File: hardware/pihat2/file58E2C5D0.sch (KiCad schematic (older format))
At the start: 45 parts, among them P1 USB_OTG, P2 BATT, P3 THERM, U1 MCP73833, U2 SMA_Edge_Mount, U3 SMA_Edge_Mount, U4 TPS61027, U5 MCP3021, U6 Si4464, U7 30MHz

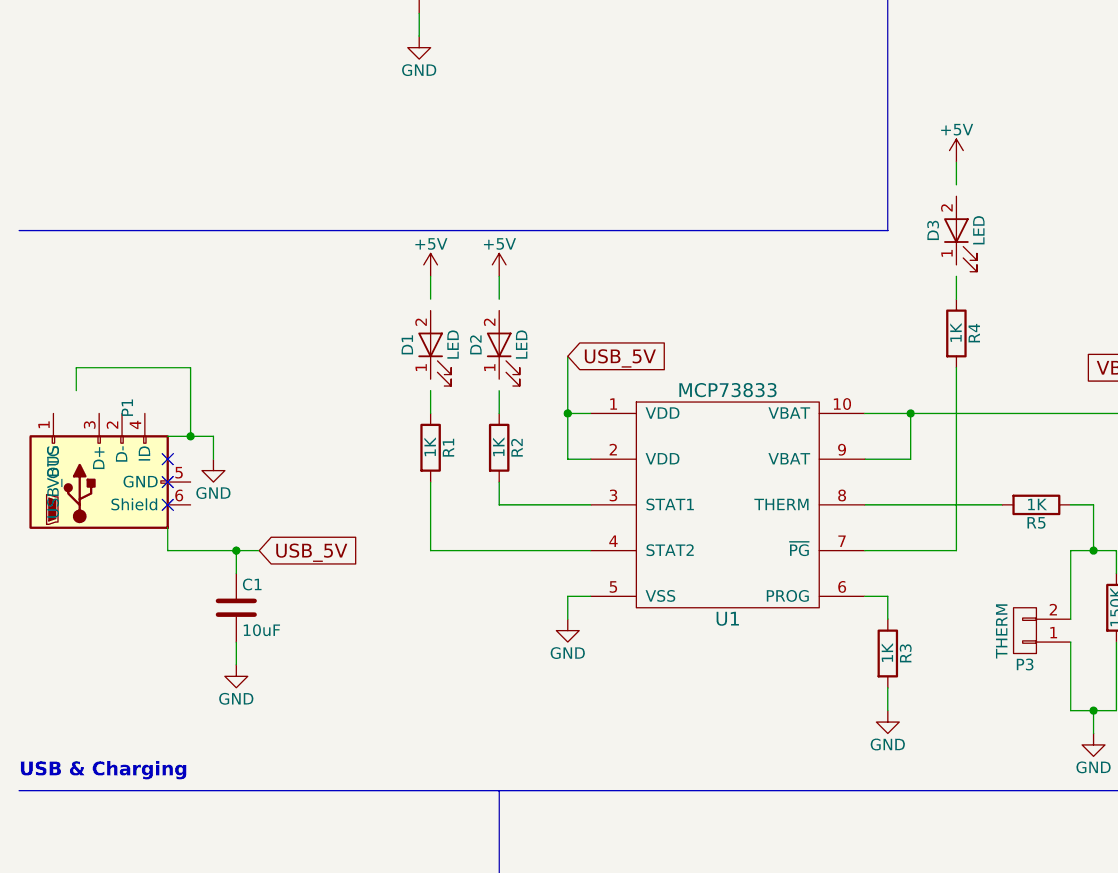
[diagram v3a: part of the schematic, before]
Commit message: Fixed some Schematic update changes that KiCAD pushed on us.
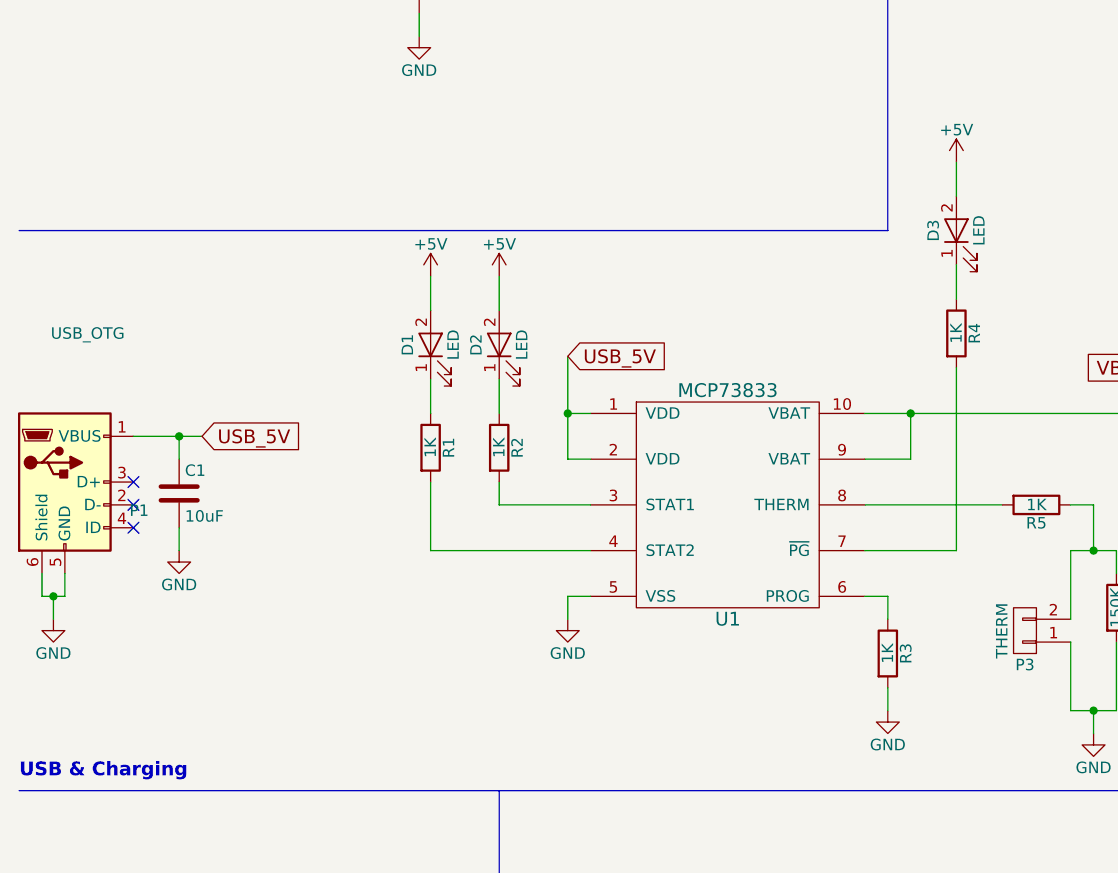
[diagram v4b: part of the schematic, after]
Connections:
- wire segments 168 -> 166
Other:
- moved on the sheet: C1, P1
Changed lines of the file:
@@
 L USB_OTG P1
 U 1 1 58E2C8C1
-P 850 3900
-F 0 "P1" H 1175 3775 50  0000 C CNN
-F 1 "USB_OTG" H 850 4100 50  0000 C CNN
-F 2 "Connect:USB_Micro-B" V 800 3800 50  0001 C CNN
-F 3 "" V 800 3800 50  0000 C CNN
-	1    850  3900
-	0    -1   -1   0
-$EndComp
-NoConn ~ 1150 3800
-NoConn ~ 1150 3900
-NoConn ~ 1150 4000
-Wire Wire Line
-	750  3500 750  3400
-Wire Wire Line
-	750  3400 1250 3400
-Wire Wire Line
-	1250 3400 1250 3700
-Wire Wire Line
-	1150 3700 1350 3700
-Wire Wire Line
-	1150 4100 1150 4200
-Wire Wire Line
-	1150 4200 1550 4200
-Wire Wire Line
-	1350 3700 1350 3800
-Connection ~ 1250 3700
-$Comp
-L GND #PWR014
-U 1 1 58E2C8C2
-P 1350 3800
-F 0 "#PWR014" H 1350 3550 50  0001 C CNN
-F 1 "GND" H 1350 3650 50  0000 C CNN
-F 2 "" H 1350 3800 50  0000 C CNN
-F 3 "" H 1350 3800 50  0000 C CNN
-	1    1350 3800
+P 700 3900
+F 0 "P1" H 1025 3775 50  0000 C CNN
+F 1 "USB_OTG" H 800 4550 50  0000 C CNN
+F 2 "Connect:USB_Micro-B" V 650 3800 50  0001 C CNN
+F 3 "" V 650 3800 50  0000 C CNN
+	1    700  3900
 	1    0    0    -1
 $EndComp
@@
 L C C1
 U 1 1 58E2C8C3
-P 1450 4450
-F 0 "C1" H 1475 4550 50  0000 L CNN
-F 1 "10uF" H 1475 4350 50  0000 L CNN
-F 2 "Capacitors_SMD:C_0805" H 1488 4300 50  0001 C CNN
-F 3 "" H 1450 4450 50  0000 C CNN
-	1    1450 4450
-	1    0    0    -1
-$EndComp
-Wire Wire Line
-	1450 4200 1450 4300
-Wire Wire Line
-	1450 4600 1450 4700
-$Comp
-L GND #PWR015
-U 1 1 58E2C8C4
-P 1450 4700
-F 0 "#PWR015" H 1450 4450 50  0001 C CNN
-F 1 "GND" H 1450 4550 50  0000 C CNN
-F 2 "" H 1450 4700 50  0000 C CNN
-F 3 "" H 1450 4700 50  0000 C CNN
-	1    1450 4700
-	1    0    0    -1
-$EndComp
-Connection ~ 1450 4200
+P 1200 3950
+F 0 "C1" H 1225 4050 50  0000 L CNN
+F 1 "10uF" H 1225 3850 50  0000 L CNN
+F 2 "Capacitors_SMD:C_0805" H 1238 3800 50  0001 C CNN
+F 3 "" H 1200 3950 50  0000 C CNN
+	1    1200 3950
+	1    0    0    -1
+$EndComp
 Wire Bus Line
 	500  2800 4300 2800
@@
 	2600 4000 3000 4000
 Wire Wire Line
-	2600 3000 2600 3100
+	2600 3000 2600 3150
 $Comp
 L R R1
@@
 	2300 4200 3000 4200
 Wire Wire Line
-	2300 3100 2300 3000
+	2300 3000 2300 3150
 Wire Wire Line
 	3000 4400 2900 4400
@@
 $EndComp
 Wire Wire Line
-	4600 3100 4600 3000
+	4600 2950 4600 3100
 $Comp
 L LED D3
@@
 $EndComp
 Wire Wire Line
-	4600 2500 4600 2600
+	4600 2500 4600 2650
 $Comp
 L R R5
@@
 	2750 1550 2850 1550
 Wire Wire Line
-	2300 3500 2300 3600
-Wire Wire Line
-	2600 3600 2600 3500
+	2300 3450 2300 3600
+Wire Wire Line
+	2600 3450 2600 3600
 $Comp
 L CONN_01X02 P3
@@
 Text GLabel 2900 3350 2    60   Input ~ 0
 USB_5V
-Text GLabel 1550 4200 2    60   Input ~ 0
+Text GLabel 1300 3700 2    60   Input ~ 0
 USB_5V
+Wire Wire Line
+	600  4300 600  4400
+Wire Wire Line
+	600  4400 700  4400
+Wire Wire Line
+	700  4400 700  4300
+Wire Wire Line
+	650  4400 650  4500
+Connection ~ 650  4400
+$Comp
+L GND #PWR?
+U 1 1 59013D1A
+P 650 4500
+F 0 "#PWR?" H 650 4250 50  0001 C CNN
+F 1 "GND" H 650 4350 50  0000 C CNN
+F 2 "" H 650 4500 50  0001 C CNN
+F 3 "" H 650 4500 50  0001 C CNN
+	1    650  4500
+	1    0    0    -1
+$EndComp
+NoConn ~ 1000 3900
+NoConn ~ 1000 4000
+NoConn ~ 1000 4100
+Wire Wire Line
+	1200 3800 1200 3700
+Wire Wire Line
+	1000 3700 1300 3700
+Connection ~ 1200 3700
+Wire Wire Line
+	1200 4100 1200 4200
+$Comp
+L GND #PWR?
+U 1 1 590142DB
+P 1200 4200
+F 0 "#PWR?" H 1200 3950 50  0001 C CNN
+F 1 "GND" H 1200 4050 50  0000 C CNN
+F 2 "" H 1200 4200 50  0001 C CNN
+F 3 "" H 1200 4200 50  0001 C CNN
+	1    1200 4200
+	1    0    0    -1
+$EndComp
 $EndSCHEMATC
